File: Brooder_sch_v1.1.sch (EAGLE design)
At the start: 37 parts, among them J1 DCJ0202, J2 1X2-3.5MM, J3 DCJ0202, J4 1X2-3.5MM, T1 2N2222, U1 328P

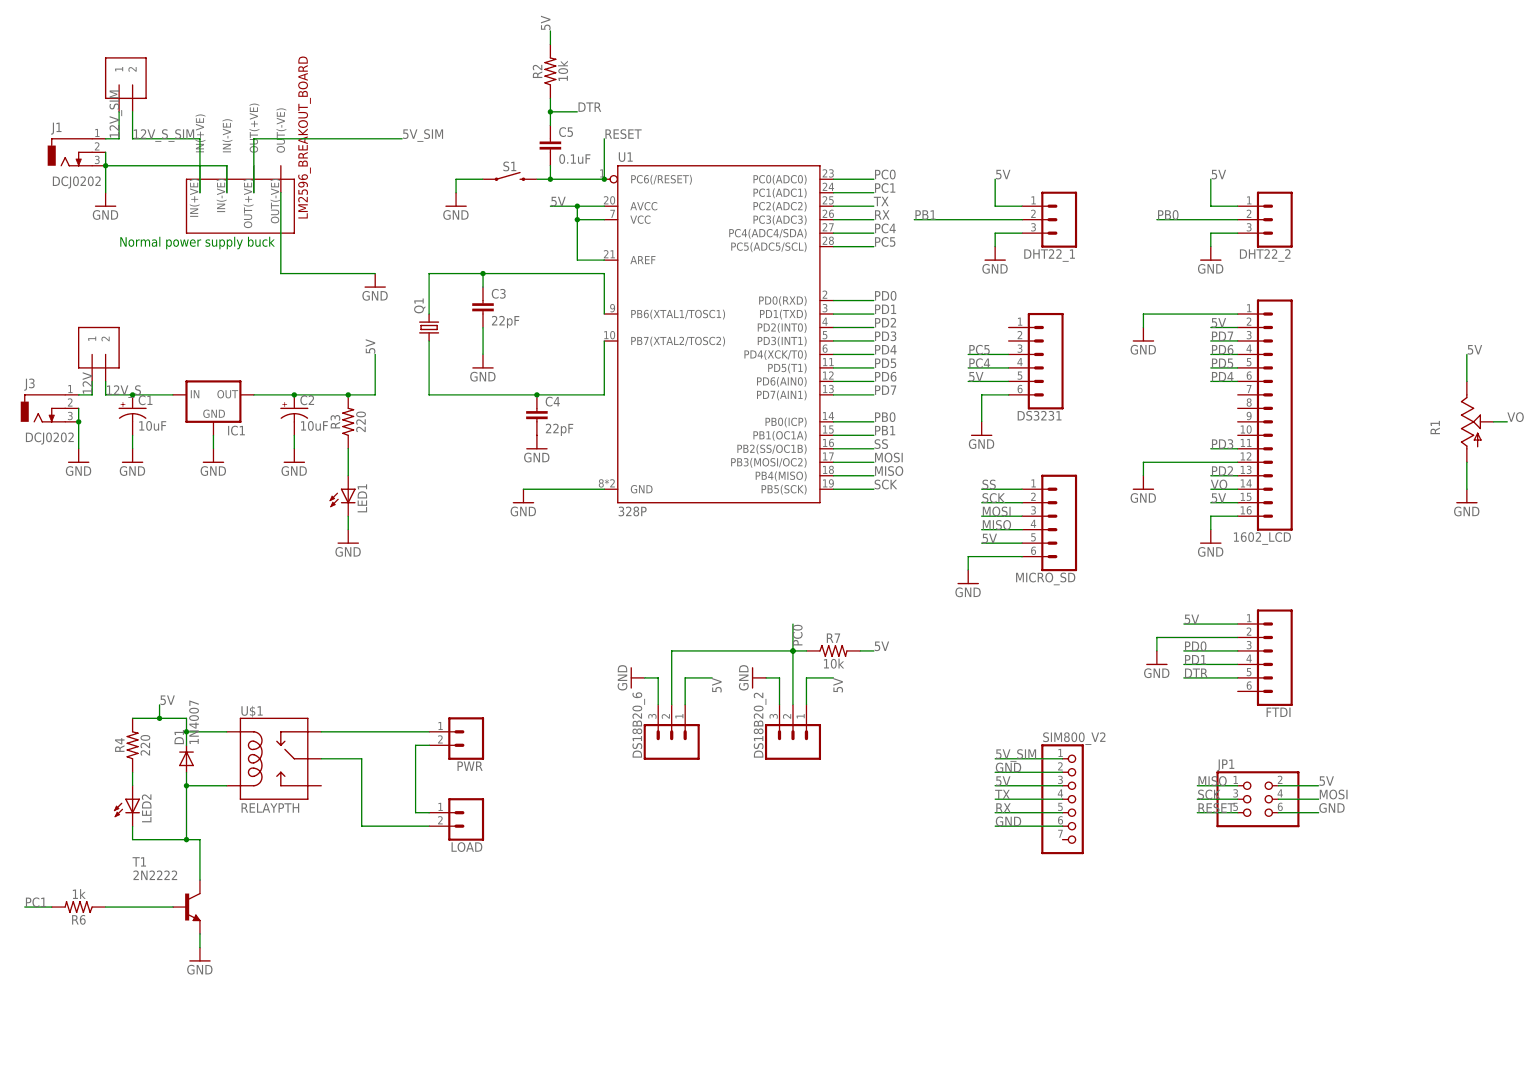
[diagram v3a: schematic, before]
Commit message: Replaces both power jacks with header pins
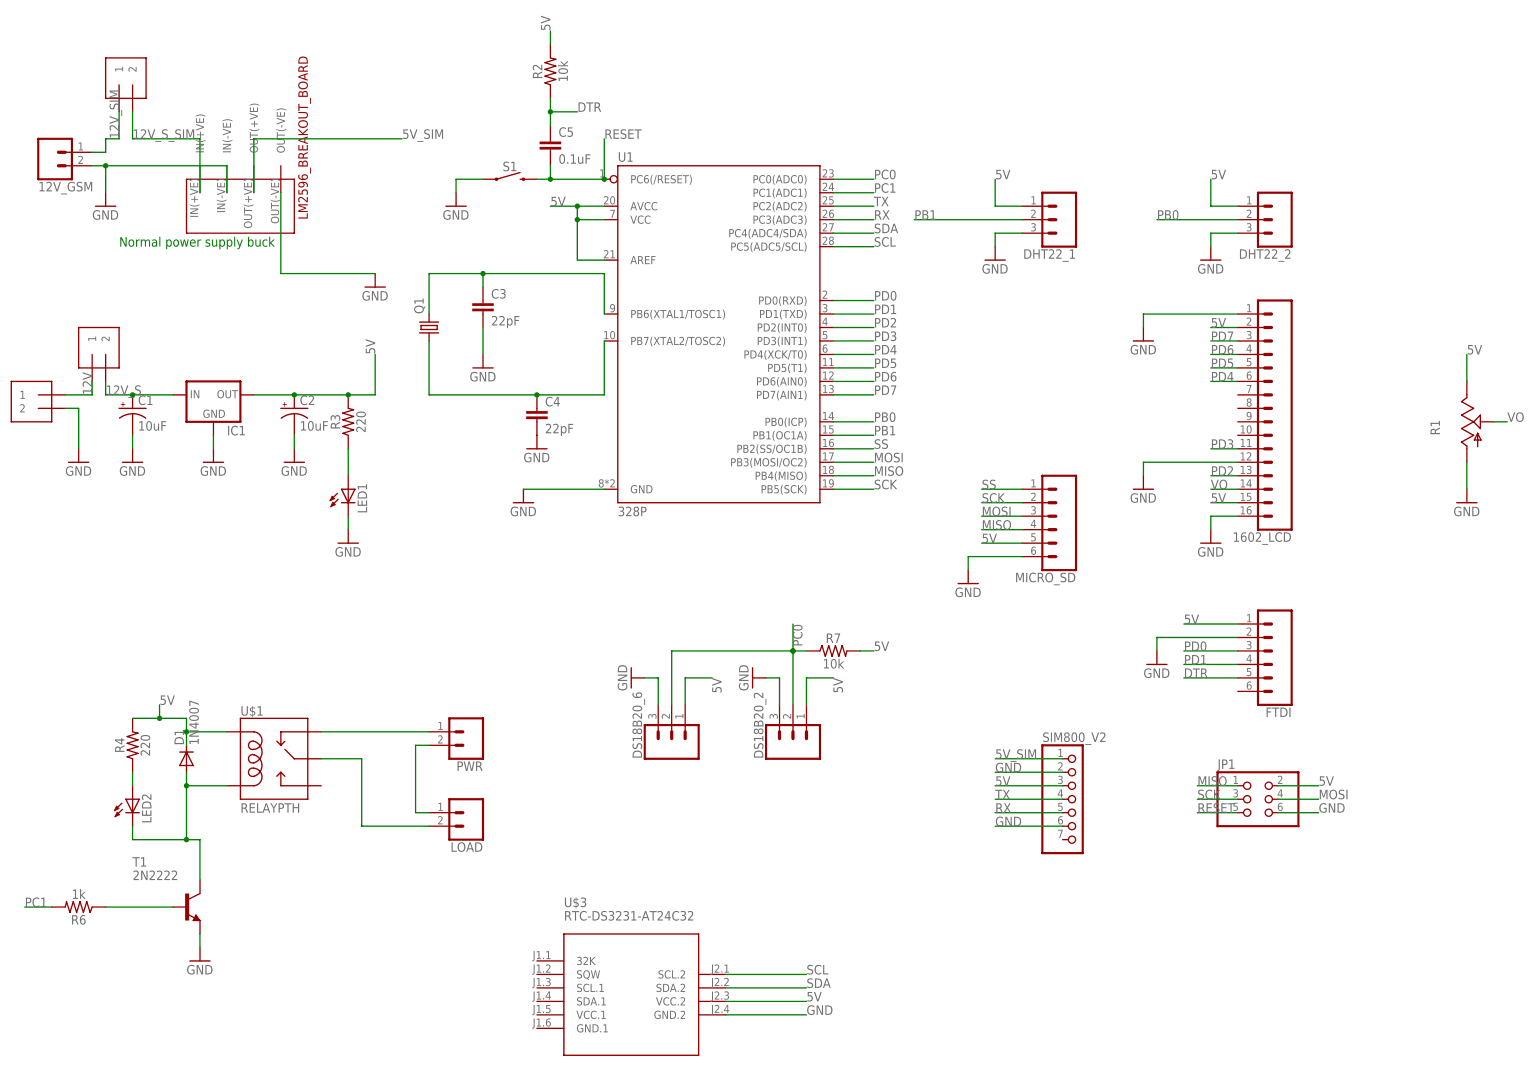
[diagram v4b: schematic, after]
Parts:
- removed DS3231: (no value), SparkFun-Connectors:CONN_06NO_SILK_FEMALE_PTH
- removed J1, J3: DCJ0202, con-jack:DCJ0202
- added 12V_GSM: (no value), SparkFun-Connectors:CONN_025MM
- added 12V_SYS: 1X2-3.5MM, adafruit:1X2-3.5MM
- added U$3: RTC-DS3231-AT24C32, diy-modules-1.8.0:RTC-DS3231-AT24C32
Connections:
- removed net PC4: DS3231.4, U1.PC4(ADC4/SDA)
- removed net PC5: DS3231.3, U1.PC5(ADC5/SCL)
- new net SCL: U$3.SCL.2, U1.PC5(ADC5/SCL)
- new net SDA: U$3.SDA.2, U1.PC4(ADC4/SDA)
- net 12V: now also 12V_SYS.1; no longer J3.1
- net 12V_SIM: now also 12V_GSM.1; no longer J1.1
- net 5V: now also U$3.VCC.2; no longer DS3231.5
- net GND: now also 12V_GSM.2, 12V_SYS.2, U$3.GND.2; no longer DS3231.6, J1.2, J1.3, J3.2, J3.3
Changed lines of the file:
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@@
 </classes>
 <parts>
-<part name="J1" library="con-jack" library_urn="urn:adsk.eagle:library:154" deviceset="DCJ0202" device="" package3d_urn="urn:adsk.eagle:package:7491/1"/>
 <part name="U1" library="SparkFun-IC-Microcontroller" deviceset="ATMEGA328P_PDIP" device="" value="328P"/>
 <part name="Q1" library="adafruit" deviceset="CRYSTAL" device="HC49S"/>
@@
 <part name="GND18" library="supply1" library_urn="urn:adsk.eagle:library:371" deviceset="GND" device=""/>
 <part name="J2" library="adafruit" deviceset="1X2" device="-3.5MM"/>
-<part name="DS3231" library="SparkFun-Connectors" deviceset="CONN_06" device="NO_SILK_FEMALE_PTH"/>
-<part name="GND25" library="supply1" library_urn="urn:adsk.eagle:library:371" deviceset="GND" device=""/>
 <part name="U$2" library="LM2596_BREAKOUT_BOARD" deviceset="LM2596_BREAKOUT_BOARD" device="THROUGH_HOLE"/>
 <part name="SIM800_V2" library="pinhead" deviceset="PINHD-1X7" device=""/>
-<part name="J3" library="con-jack" library_urn="urn:adsk.eagle:library:154" deviceset="DCJ0202" device="" package3d_urn="urn:adsk.eagle:package:7491/1"/>
 <part name="C1" library="SparkFun-Capacitors" deviceset="10UF-POLAR" device="-RADIAL-2.5MM-25V-20%" value="10uF"/>
 <part name="C2" library="SparkFun-Capacitors" deviceset="10UF-POLAR" device="-RADIAL-2.5MM-25V-20%" value="10uF"/>
@@
 <part name="GND22" library="supply1" library_urn="urn:adsk.eagle:library:371" deviceset="GND" device=""/>
 <part name="LOAD" library="SparkFun-Connectors" deviceset="CONN_02" device="5MM"/>
+<part name="U$3" library="diy-modules-1.8.0" deviceset="RTC-DS3231-AT24C32" device=""/>
+<part name="12V_GSM" library="SparkFun-Connectors" deviceset="CONN_02" device="5MM"/>
+<part name="12V_SYS" library="adafruit" deviceset="1X2" device="-3.5MM"/>
 </parts>
 <sheets>
@@
 </plain>
 <instances>
-<instance part="J1" gate="G$1" x="-68.58" y="109.22" smashed="yes">
-<attribute name="NAME" x="-71.12" y="113.03" size="1.778" layer="95"/>
-<attribute name="VALUE" x="-71.12" y="102.87" size="1.778" layer="96"/>
-</instance>
 <instance part="U1" gate="U1" x="53.34" y="78.74" smashed="yes">
 <attribute name="NAME" x="35.56" y="107.442" size="1.778" layer="95"/>
@@
 </instance>
 <instance part="J2" gate="G$1" x="-55.88" y="121.92" rot="R90"/>
-<instance part="DS3231" gate="G$1" x="114.3" y="71.12" smashed="yes" rot="R180">
-<attribute name="VALUE" x="119.38" y="81.026" size="1.778" layer="96" font="vector" rot="R180"/>
-<attribute name="NAME" x="119.38" y="60.452" size="1.778" layer="95" font="vector" rot="R180"/>
-</instance>
-<instance part="GND25" gate="1" x="104.14" y="55.88" smashed="yes">
-<attribute name="VALUE" x="101.6" y="53.34" size="1.778" layer="96"/>
-</instance>
 <instance part="U$2" gate="G$1" x="-20.32" y="129.54" rot="R90"/>
 <instance part="SIM800_V2" gate="A" x="121.92" y="-12.7"/>
-<instance part="J3" gate="G$1" x="-73.66" y="60.96" smashed="yes">
-<attribute name="NAME" x="-76.2" y="64.77" size="1.778" layer="95"/>
-<attribute name="VALUE" x="-76.2" y="54.61" size="1.778" layer="96"/>
-</instance>
 <instance part="C1" gate="G$1" x="-55.88" y="60.96" smashed="yes">
 <attribute name="NAME" x="-54.864" y="61.595" size="1.778" layer="95" font="vector"/>
@@
 <attribute name="NAME" x="10.16" y="-20.828" size="1.778" layer="95" font="vector" rot="R180"/>
 </instance>
+<instance part="U$3" gate="G$1" x="38.1" y="-48.26"/>
+<instance part="12V_GSM" gate="G$1" x="-71.12" y="109.22" smashed="yes" rot="MR180">
+<attribute name="VALUE" x="-73.66" y="114.046" size="1.778" layer="96" font="vector" rot="MR180"/>
+<attribute name="NAME" x="-73.66" y="103.632" size="1.778" layer="95" font="vector" rot="MR180"/>
+</instance>
+<instance part="12V_SYS" gate="G$1" x="-73.66" y="60.96" rot="MR0"/>
 </instances>
 <busses>
@@
 <net name="GND" class="0">
 <segment>
-<pinref part="J1" gate="G$1" pin="2"/>
-<pinref part="J1" gate="G$1" pin="3"/>
-<wire x1="-60.96" y1="109.22" x2="-60.96" y2="106.68" width="0.1524" layer="91"/>
 <pinref part="GND1" gate="1" pin="GND"/>
 <wire x1="-60.96" y1="106.68" x2="-60.96" y2="101.6" width="0.1524" layer="91"/>
-<junction x="-60.96" y="106.68"/>
 <pinref part="U$2" gate="G$1" pin="IN(-VE)"/>
 <wire x1="-60.96" y1="106.68" x2="-38.1" y2="106.68" width="0.1524" layer="91"/>
 <wire x1="-38.1" y1="106.68" x2="-38.1" y2="101.6" width="0.1524" layer="91"/>
+<pinref part="12V_GSM" gate="G$1" pin="2"/>
+<wire x1="-63.5" y1="106.68" x2="-60.96" y2="106.68" width="0.1524" layer="91"/>
+<junction x="-60.96" y="106.68"/>
 </segment>
 <segment>
@@
 </segment>
 <segment>
-<pinref part="DS3231" gate="G$1" pin="6"/>
-<wire x1="109.22" y1="63.5" x2="104.14" y2="63.5" width="0.1524" layer="91"/>
-<wire x1="104.14" y1="63.5" x2="104.14" y2="58.42" width="0.1524" layer="91"/>
-<pinref part="GND25" gate="1" pin="GND"/>
-</segment>
-<segment>
 <pinref part="SIM800_V2" gate="A" pin="2"/>
 <wire x1="119.38" y1="-7.62" x2="106.68" y2="-7.62" width="0.1524" layer="91"/>
@@
 </segment>
 <segment>
-<pinref part="J3" gate="G$1" pin="2"/>
-<pinref part="J3" gate="G$1" pin="3"/>
-<wire x1="-66.04" y1="60.96" x2="-66.04" y2="58.42" width="0.1524" layer="91"/>
 <pinref part="GND2" gate="1" pin="GND"/>
-<wire x1="-66.04" y1="58.42" x2="-66.04" y2="53.34" width="0.1524" layer="91"/>
-<junction x="-66.04" y="58.42"/>
+<wire x1="-66.04" y1="60.96" x2="-66.04" y2="53.34" width="0.1524" layer="91"/>
+<pinref part="12V_SYS" gate="G$1" pin="2"/>
+<wire x1="-68.58" y1="60.96" x2="-66.04" y2="60.96" width="0.1524" layer="91"/>
 </segment>
 <segment>
@@
 <pinref part="GND22" gate="1" pin="GND"/>
 </segment>
+<segment>
+<pinref part="U$3" gate="G$1" pin="GND.2"/>
+<wire x1="55.88" y1="-53.34" x2="71.12" y2="-53.34" width="0.1524" layer="91"/>
+<label x="71.12" y="-53.34" size="1.778" layer="95"/>
+</segment>
 </net>
 <net name="12V" class="0">
 <segment>
-<pinref part="J3" gate="G$1" pin="1"/>
-<wire x1="-66.04" y1="63.5" x2="-63.5" y2="63.5" width="0.1524" layer="91"/>
 <pinref part="J4" gate="G$1" pin="1"/>
 <wire x1="-63.5" y1="63.5" x2="-63.5" y2="66.04" width="0.1524" layer="91"/>
 <label x="-63.5" y="63.5" size="1.778" layer="95" rot="R90"/>
+<pinref part="12V_SYS" gate="G$1" pin="1"/>
+<wire x1="-68.58" y1="63.5" x2="-63.5" y2="63.5" width="0.1524" layer="91"/>
 </segment>
 </net>
@@
 </segment>
 <segment>
-<pinref part="DS3231" gate="G$1" pin="5"/>
-<wire x1="109.22" y1="66.04" x2="101.6" y2="66.04" width="0.1524" layer="91"/>
-<label x="101.6" y="66.04" size="1.778" layer="95"/>
-</segment>
-<segment>
 <pinref part="SIM800_V2" gate="A" pin="3"/>
 <wire x1="119.38" y1="-10.16" x2="106.68" y2="-10.16" width="0.1524" layer="91"/>
@@
 <label x="-50.8" y="5.08" size="1.778" layer="95"/>
 </segment>
+<segment>
+<pinref part="U$3" gate="G$1" pin="VCC.2"/>
+<wire x1="55.88" y1="-50.8" x2="71.12" y2="-50.8" width="0.1524" layer="91"/>
+<label x="71.12" y="-50.8" size="1.778" layer="95"/>
+</segment>
 </net>
 <net name="N$5" class="0">
@@
 </segment>
 </net>
-<net name="PC4" class="0">
-<segment>
-<pinref part="DS3231" gate="G$1" pin="4"/>
-<wire x1="109.22" y1="68.58" x2="101.6" y2="68.58" width="0.1524" layer="91"/>
-<label x="101.6" y="68.58" size="1.778" layer="95"/>
-</segment>
-<segment>
-<pinref part="U1" gate="U1" pin="PC4(ADC4/SDA)"/>
-<wire x1="76.2" y1="93.98" x2="83.82" y2="93.98" width="0.1524" layer="91"/>
-<label x="83.82" y="93.98" size="1.778" layer="95"/>
-</segment>
-</net>
-<net name="PC5" class="0">
-<segment>
-<pinref part="DS3231" gate="G$1" pin="3"/>
-<wire x1="109.22" y1="71.12" x2="101.6" y2="71.12" width="0.1524" layer="91"/>
-<label x="101.6" y="71.12" size="1.778" layer="95"/>
-</segment>
-<segment>
-<pinref part="U1" gate="U1" pin="PC5(ADC5/SCL)"/>
-<wire x1="76.2" y1="91.44" x2="83.82" y2="91.44" width="0.1524" layer="91"/>
-<label x="83.82" y="91.44" size="1.778" layer="95"/>
-</segment>
-</net>
 <net name="TX" class="0">
 <segment>
@@
 <net name="12V_SIM" class="0">
 <segment>
-<pinref part="J1" gate="G$1" pin="1"/>
 <wire x1="-60.96" y1="111.76" x2="-58.42" y2="111.76" width="0.1524" layer="91"/>
 <pinref part="J2" gate="G$1" pin="1"/>
 <wire x1="-58.42" y1="111.76" x2="-58.42" y2="116.84" width="0.1524" layer="91"/>
 <label x="-58.42" y="111.76" size="1.778" layer="95" rot="R90"/>
+<pinref part="12V_GSM" gate="G$1" pin="1"/>
+<wire x1="-63.5" y1="109.22" x2="-60.96" y2="109.22" width="0.1524" layer="91"/>
+<wire x1="-60.96" y1="109.22" x2="-60.96" y2="111.76" width="0.1524" layer="91"/>
 </segment>
 </net>
@@
 </segment>
 </net>
+<net name="SCL" class="0">
+<segment>
+<pinref part="U$3" gate="G$1" pin="SCL.2"/>
+<wire x1="55.88" y1="-45.72" x2="71.12" y2="-45.72" width="0.1524" layer="91"/>
+<label x="71.12" y="-45.72" size="1.778" layer="95"/>
+</segment>
+<segment>
+<pinref part="U1" gate="U1" pin="PC5(ADC5/SCL)"/>
+<wire x1="76.2" y1="91.44" x2="83.82" y2="91.44" width="0.1524" layer="91"/>
+<label x="83.82" y="91.44" size="1.778" layer="95"/>
+</segment>
+</net>
+<net name="SDA" class="0">
+<segment>
+<pinref part="U$3" gate="G$1" pin="SDA.2"/>
+<wire x1="55.88" y1="-48.26" x2="71.12" y2="-48.26" width="0.1524" layer="91"/>
+<label x="71.12" y="-48.26" size="1.778" layer="95"/>
+</segment>
+<segment>
+<pinref part="U1" gate="U1" pin="PC4(ADC4/SDA)"/>
+<wire x1="76.2" y1="93.98" x2="83.82" y2="93.98" width="0.1524" layer="91"/>
+<label x="83.82" y="93.98" size="1.778" layer="95"/>
+</segment>
+</net>

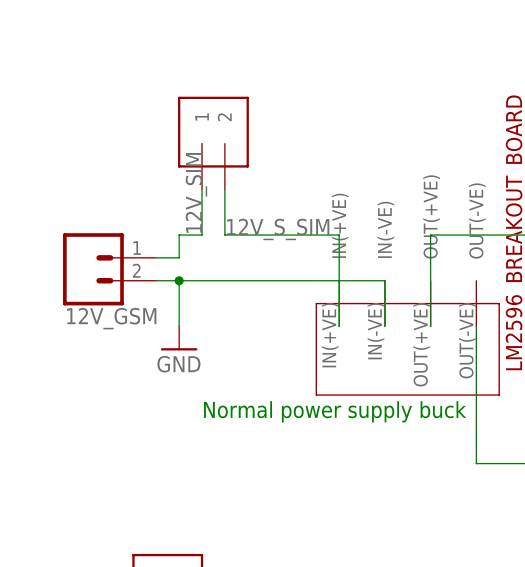
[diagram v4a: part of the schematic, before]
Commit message: Adds custom sim800V2 library symbol to schematic
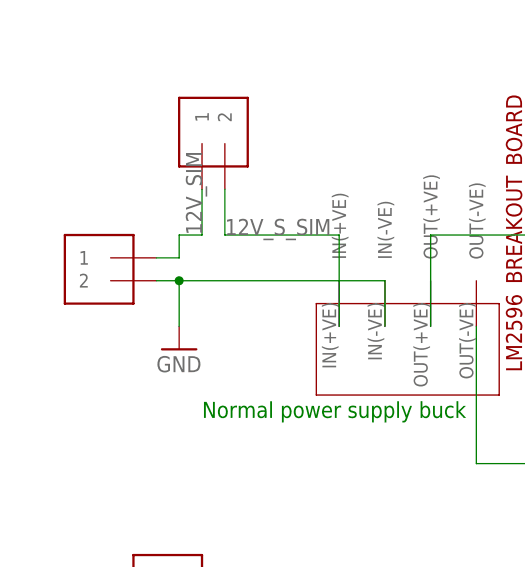
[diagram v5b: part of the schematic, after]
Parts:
- 12V_GSM: value (none) -> 1X2-3.5MM; device SparkFun-Connectors:CONN_025MM -> adafruit:1X2-3.5MM
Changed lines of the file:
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@@
 <part name="LOAD" library="SparkFun-Connectors" deviceset="CONN_02" device="5MM"/>
 <part name="U$3" library="diy-modules-1.8.0" deviceset="RTC-DS3231-AT24C32" device=""/>
-<part name="12V_GSM" library="SparkFun-Connectors" deviceset="CONN_02" device="5MM"/>
 <part name="12V_SYS" library="adafruit" deviceset="1X2" device="-3.5MM"/>
+<part name="12V_GSM" library="adafruit" deviceset="1X2" device="-3.5MM"/>
 </parts>
 <sheets>
@@
 </instance>
 <instance part="U$3" gate="G$1" x="38.1" y="-48.26"/>
-<instance part="12V_GSM" gate="G$1" x="-71.12" y="109.22" smashed="yes" rot="MR180">
-<attribute name="VALUE" x="-73.66" y="114.046" size="1.778" layer="96" font="vector" rot="MR180"/>
-<attribute name="NAME" x="-73.66" y="103.632" size="1.778" layer="95" font="vector" rot="MR180"/>
-</instance>
 <instance part="12V_SYS" gate="G$1" x="-73.66" y="60.96" rot="MR0"/>
+<instance part="12V_GSM" gate="G$1" x="-68.58" y="106.68" rot="MR0"/>
 </instances>
 <busses>
@@
 <wire x1="-60.96" y1="106.68" x2="-38.1" y2="106.68" width="0.1524" layer="91"/>
 <wire x1="-38.1" y1="106.68" x2="-38.1" y2="101.6" width="0.1524" layer="91"/>
-<pinref part="12V_GSM" gate="G$1" pin="2"/>
 <wire x1="-63.5" y1="106.68" x2="-60.96" y2="106.68" width="0.1524" layer="91"/>
 <junction x="-60.96" y="106.68"/>
+<pinref part="12V_GSM" gate="G$1" pin="2"/>
 </segment>
 <segment>
@@
 <wire x1="-58.42" y1="111.76" x2="-58.42" y2="116.84" width="0.1524" layer="91"/>
 <label x="-58.42" y="111.76" size="1.778" layer="95" rot="R90"/>
-<pinref part="12V_GSM" gate="G$1" pin="1"/>
 <wire x1="-63.5" y1="109.22" x2="-60.96" y2="109.22" width="0.1524" layer="91"/>
 <wire x1="-60.96" y1="109.22" x2="-60.96" y2="111.76" width="0.1524" layer="91"/>
-</segment>
-</net>
+<pinref part="12V_GSM" gate="G$1" pin="1"/>
+</segment>
+</net>
